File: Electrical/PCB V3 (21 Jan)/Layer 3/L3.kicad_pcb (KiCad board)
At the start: 2 copper layers, 129.9 x 119.9 mm, 28 parts, among them J1 Conn_01x06, J2 Conn_02x04_Counter_Clockwise, J3 Conn_01x06, J4 Conn_01x06, J5 Conn_01x06, U2 113991054, U3 4754

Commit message: did some stuff with l3, settke another day
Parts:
- J2: value Conn_02x04_Counter_Clockwise -> Conn_02x04_Odd_Even
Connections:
- J2 pad 2: /TX (L3 ESP32) -> /TX (CAM)
- J2 pad 3: /RX (L3 ESP32) -> /TX (L3 ESP32)
- J2 pad 4: GND -> /RX (CAM)
- J2 pad 5: /RX (IMU) -> /RX (L3 ESP32)
- J2 pad 7: /RX (CAM) -> GND
- J2 pad 8: /TX (CAM) -> /RX (IMU)
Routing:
- net /RX (L3 ESP32): track 83.0 -> 94.4 mm
- net /RX (CAM): track 81.5 -> 72.0 mm
- net /TX (CAM): track 83.2 -> 75.1 mm
- net +3V3: track 351.9 -> 347.5 mm
- net /TX (L3 ESP32): track 81.0 -> 77.0 mm
- net /RX (IMU): track 38.7 -> 41.5 mm
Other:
- board text added: "{dblquote} 'i like this trace' vincent 2025 {dblquote} - haoyuan 2025"
- board text added: "{dblquote}does he know theres another side to the pcb{dblquote} - somebody 2025"

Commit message: uncursed l3
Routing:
- net +3V3: track 347.5 -> 326.6 mm, vias 2 -> 8
- net /TOF3 XSHUT: track 134.1 -> 116.9 mm
- net /TOF2 XSHUT: track 66.5 -> 50.4 mm
- net /TOF1 XSHUT: track 122.0 -> 111.5 mm
- net /SDA: track 225.3 -> 224.7 mm
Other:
- board text removed: "{dblquote} 'i like this trace' vincent 2025 {dblquote} - haoyuan 2025"
- board text removed: "{dblquote}does he know theres another side to the pcb{dblquote} - somebody 2025"

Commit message: did l3 more
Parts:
- moved R1 1.00 mm to (176.3, 54.5)
- moved R2 1.00 mm to (178.9, 54.5)
- moved R3 1.00 mm to (209.9, 61.5)
- moved R4 1.00 mm to (212.5, 61.5)
- moved R5 1.00 mm to (166.2, 54.5)
- moved R6 1.00 mm to (168.7, 54.5)
- moved R7 1.00 mm to (171.3, 54.5)
- moved R8 1.00 mm to (173.8, 54.5)
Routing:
- net /SCL: track 249.4 -> 222.4 mm, vias 0 -> 3
- net /SDA: track 224.7 -> 248.0 mm
- net /TOF3 XSHUT: track 116.9 -> 103.2 mm
- net +3V3: track 326.6 -> 336.5 mm
- net /TX (IMU): track 38.8 -> 45.0 mm, vias 0 -> 1
- net /TOF1 XSHUT: track 111.5 -> 117.4 mm
- net /TX (CAM): track 75.1 -> 80.9 mm
- net /TOF2 XSHUT: track 50.4 -> 53.7 mm
- net /RX (L3 ESP32): track 94.4 -> 96.5 mm, vias 0 -> 2
- net /RX (IMU): track 41.5 -> 43.3 mm
- net /TOF4 XSHUT: track 56.9 -> 58.6 mm
- net Net-(U3-P1): track 2.29 -> 3.29 mm
- net Net-(U3-P0): track 2.29 -> 3.29 mm
- net GND: vias 2 -> 0

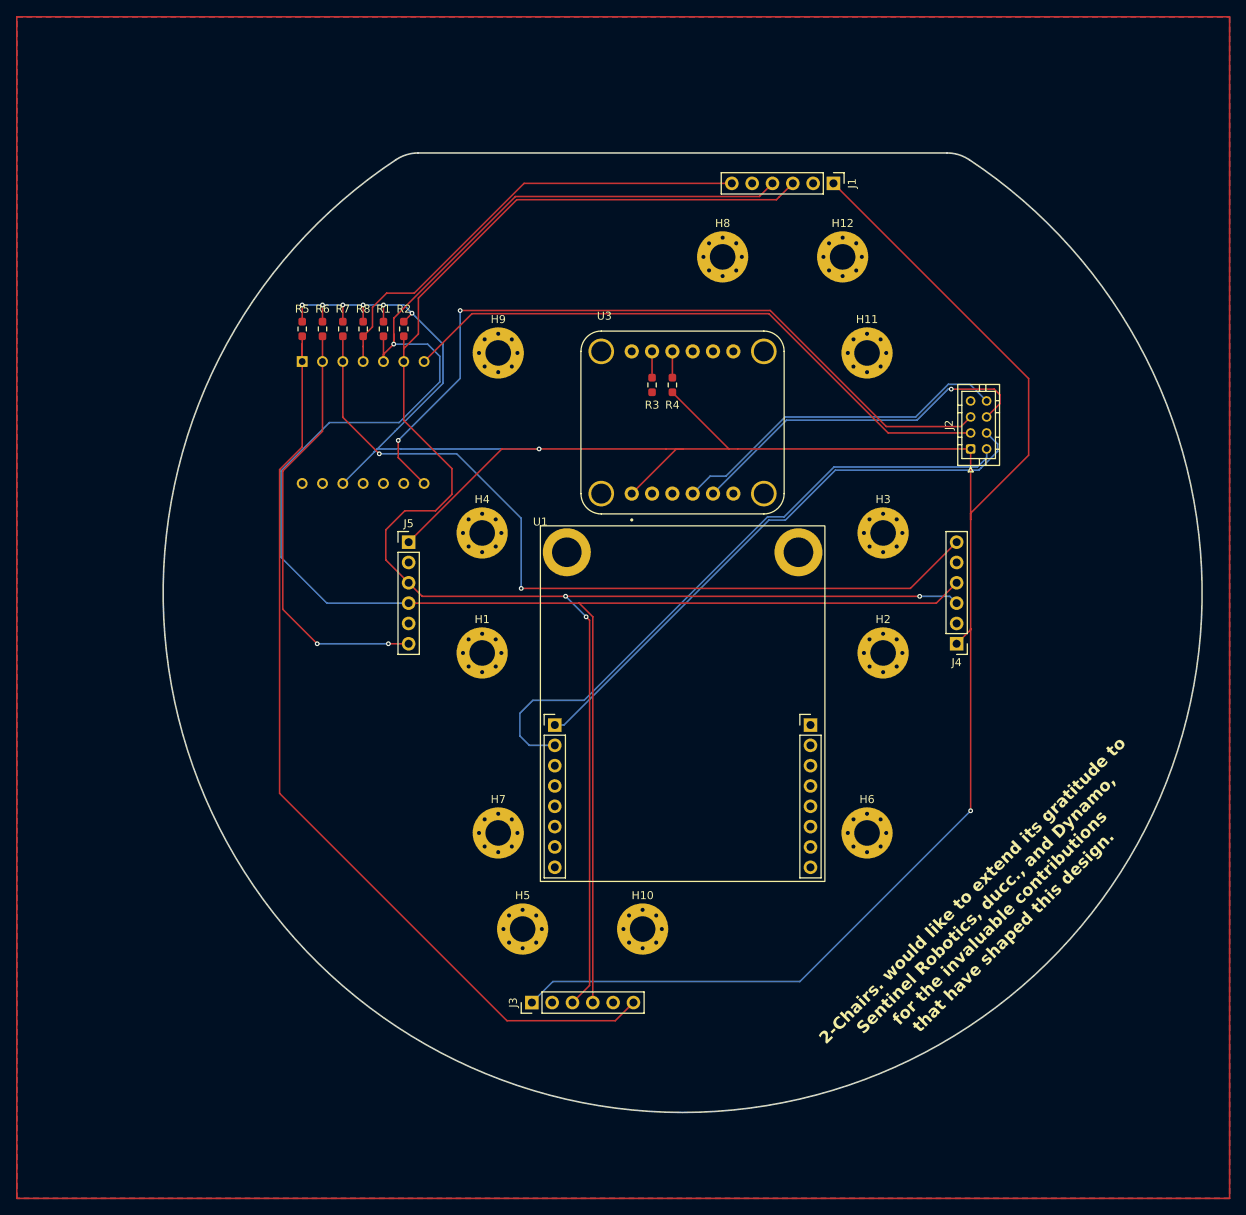
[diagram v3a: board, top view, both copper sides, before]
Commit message: spaced out l3 traces
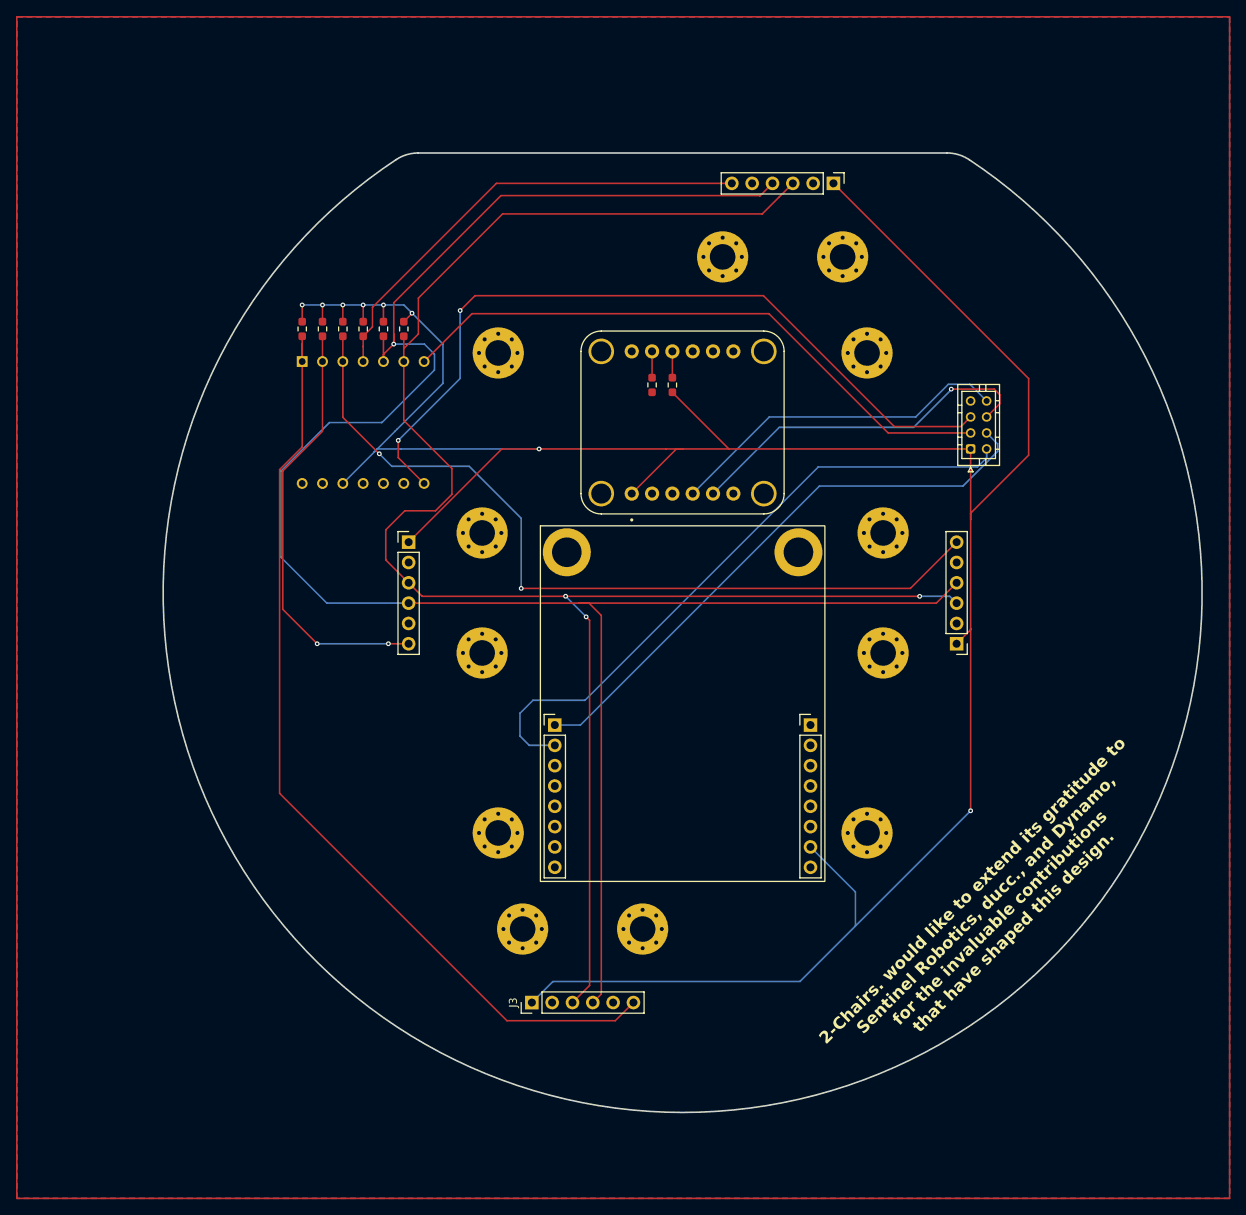
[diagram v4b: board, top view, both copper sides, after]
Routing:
- net +3V3: track 336.5 -> 348.7 mm
- net /RX (L3 ESP32): track 96.5 -> 98.0 mm
- net /SDA: track 248.0 -> 248.8 mm

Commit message: fixed l1 and l3, awaiting vetting
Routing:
- net +3V3: track 348.7 -> 369.2 mm
- net /TX (CAM): track 80.9 -> 71.2 mm, vias 0 -> 1
- net /SCL: track 222.4 -> 218.5 mm, vias 3 -> 4
- net /RX (L3 ESP32): track 98.0 -> 95.0 mm
- net /SDA: track 248.8 -> 249.9 mm
- net /TOF1 XSHUT: track 117.4 -> 116.4 mm
- net /RX (CAM): track 72.4 -> 73.3 mm
- net /TX (IMU): track 45.1 -> 45.7 mm
- net /TOF2 XSHUT: track 53.7 -> 54.1 mm, vias 2 -> 0
- net GND: vias 0 -> 103

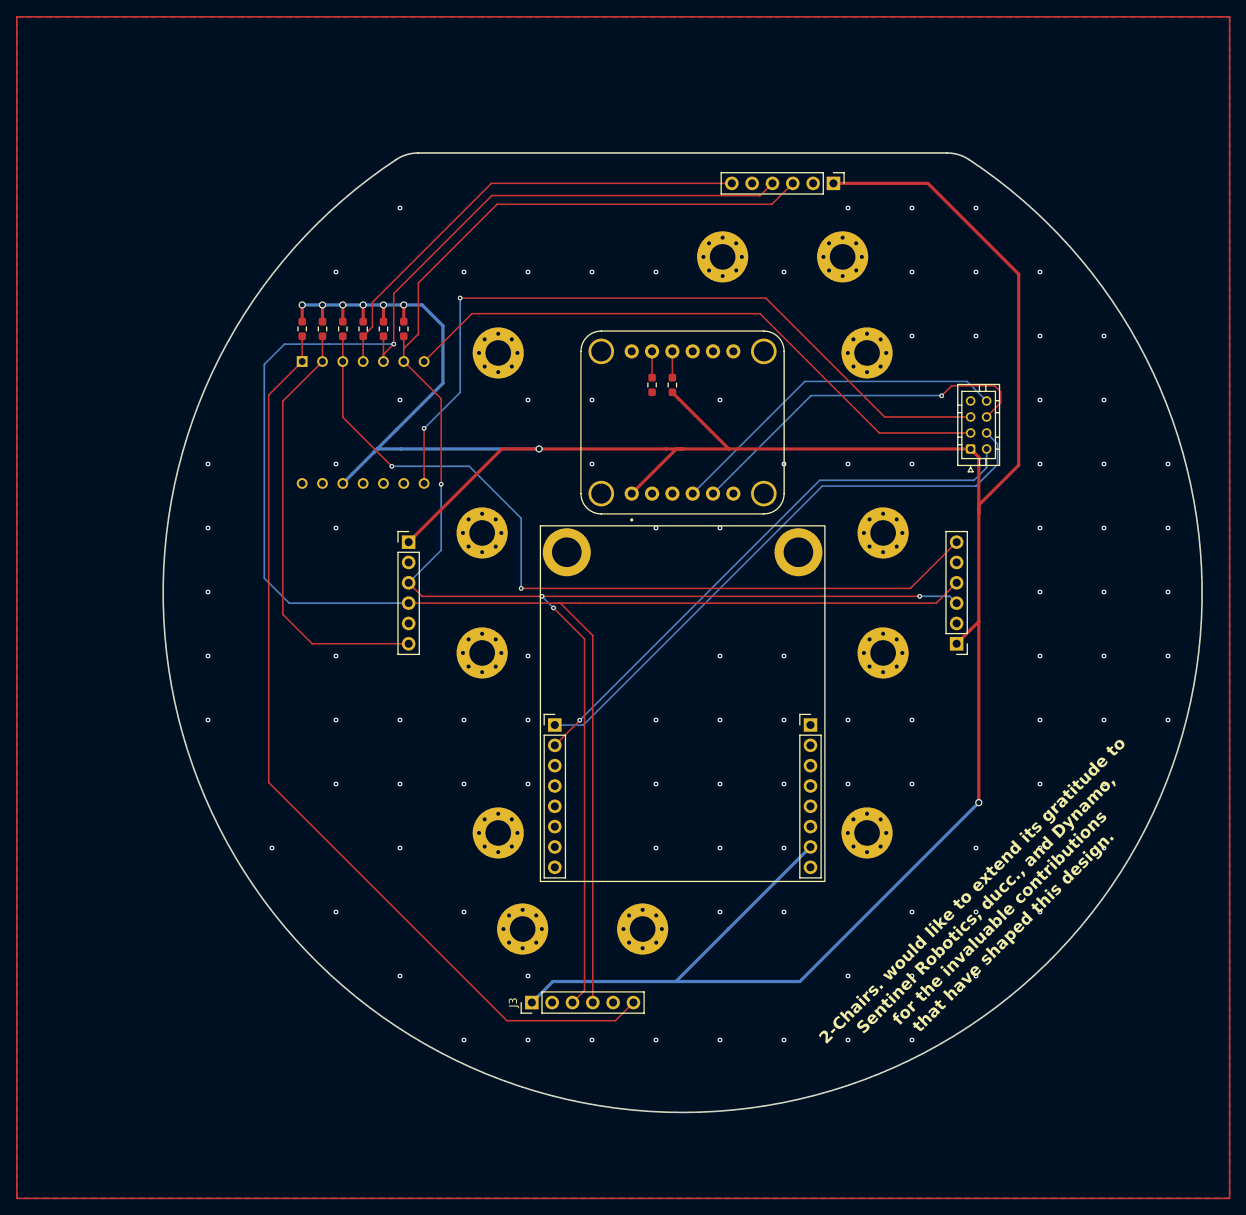
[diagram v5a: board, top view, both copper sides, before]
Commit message: L1 & L3 APPROVED BY HAOYUN
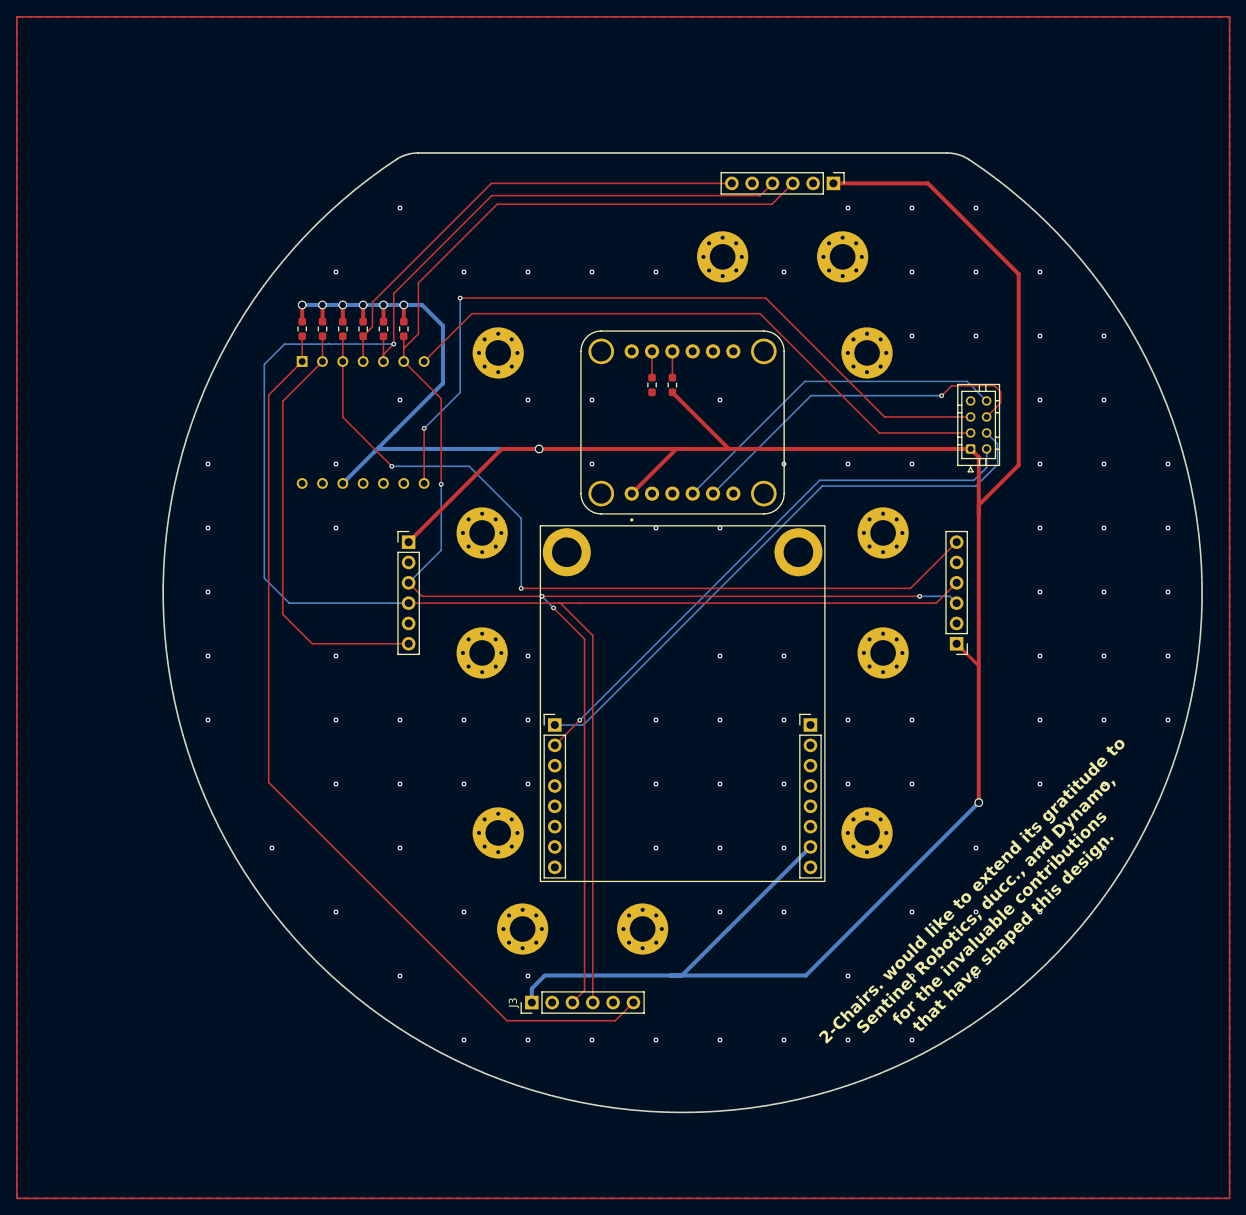
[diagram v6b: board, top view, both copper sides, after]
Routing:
- net +3V3: track 369.2 -> 371.8 mm

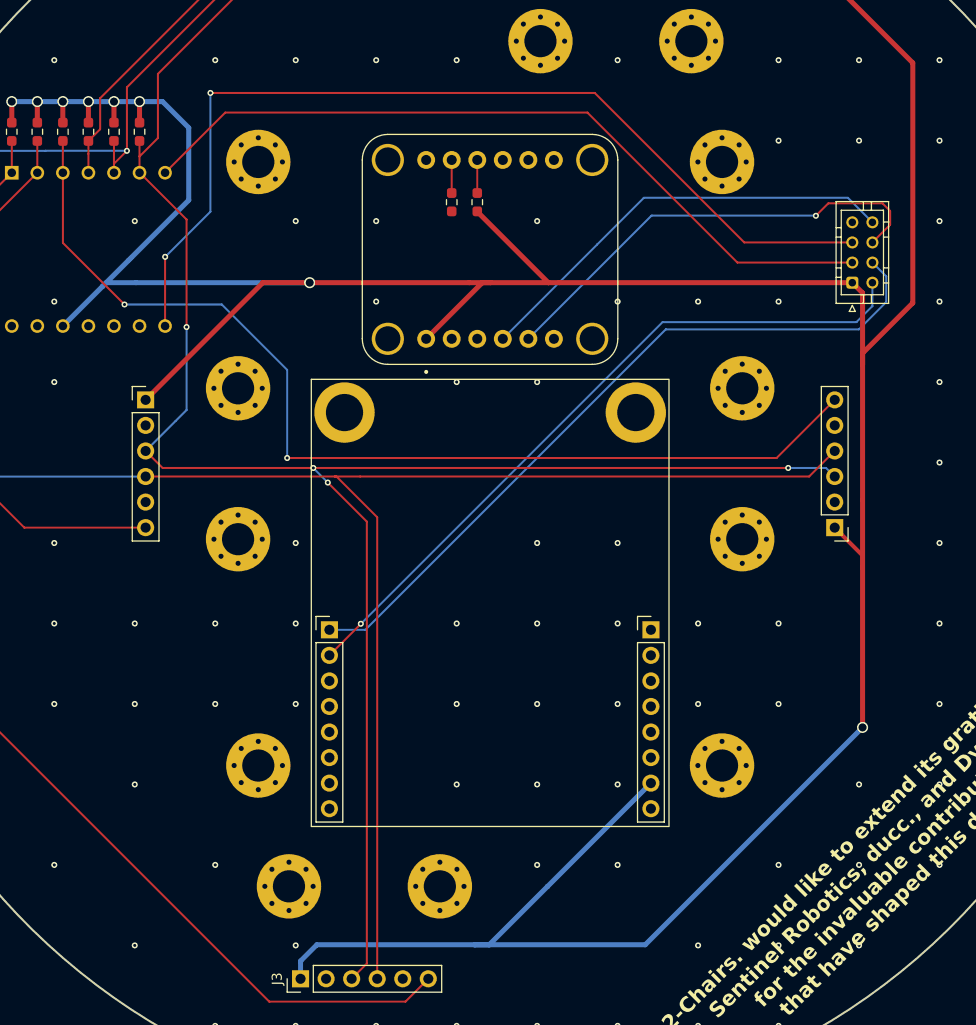
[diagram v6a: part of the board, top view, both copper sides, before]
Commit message: removed acute angles from l3
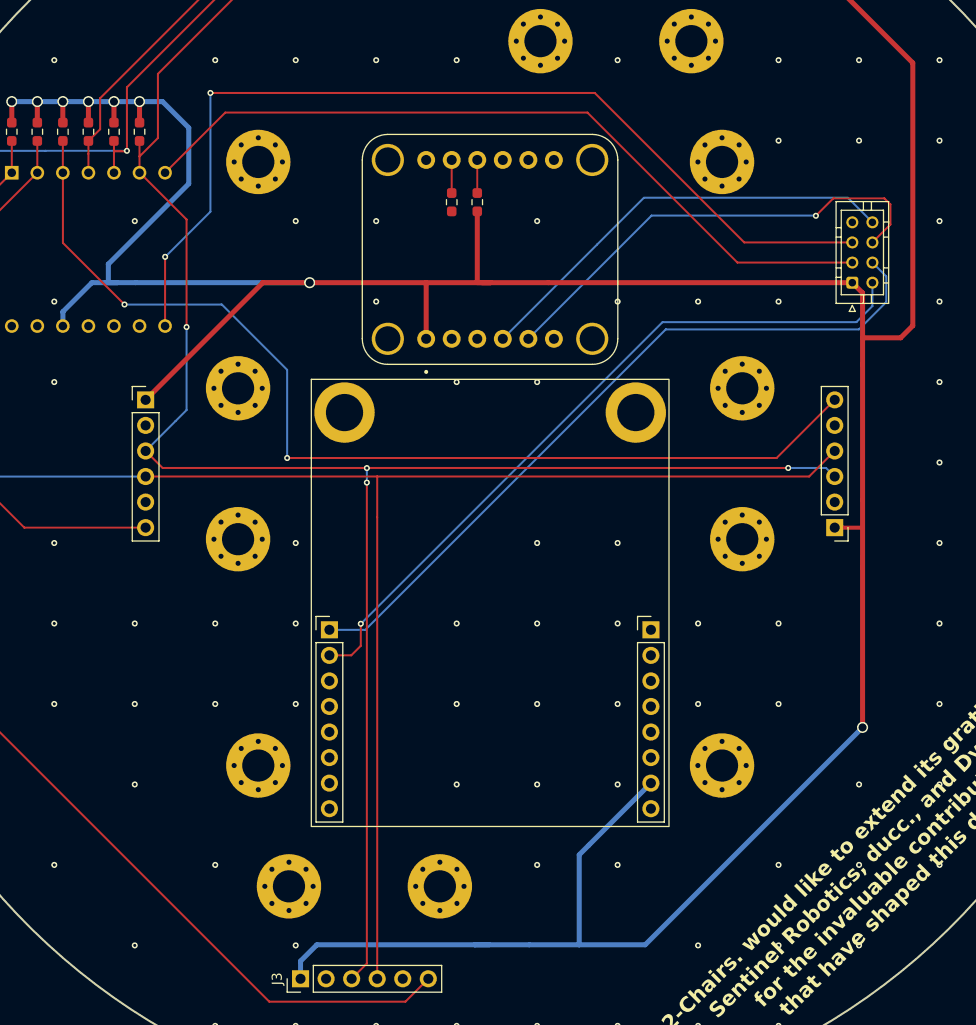
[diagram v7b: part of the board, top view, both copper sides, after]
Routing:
- net +3V3: track 371.8 -> 363.7 mm
- net /SDA: track 249.9 -> 246.6 mm
- net /SCL: track 218.5 -> 216.3 mm
- net /TX (CAM): track 71.2 -> 72.5 mm
- net /TX (IMU): track 45.7 -> 46.6 mm
